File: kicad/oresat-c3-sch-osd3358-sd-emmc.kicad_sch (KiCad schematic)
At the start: 65 parts, among them J4 DM3BT-DSF-PEJS, U1 OSD3358-512M-BSM, U8 TCAN330, U9 EMMC+RESET+5.1-COMPATIBLE-BA

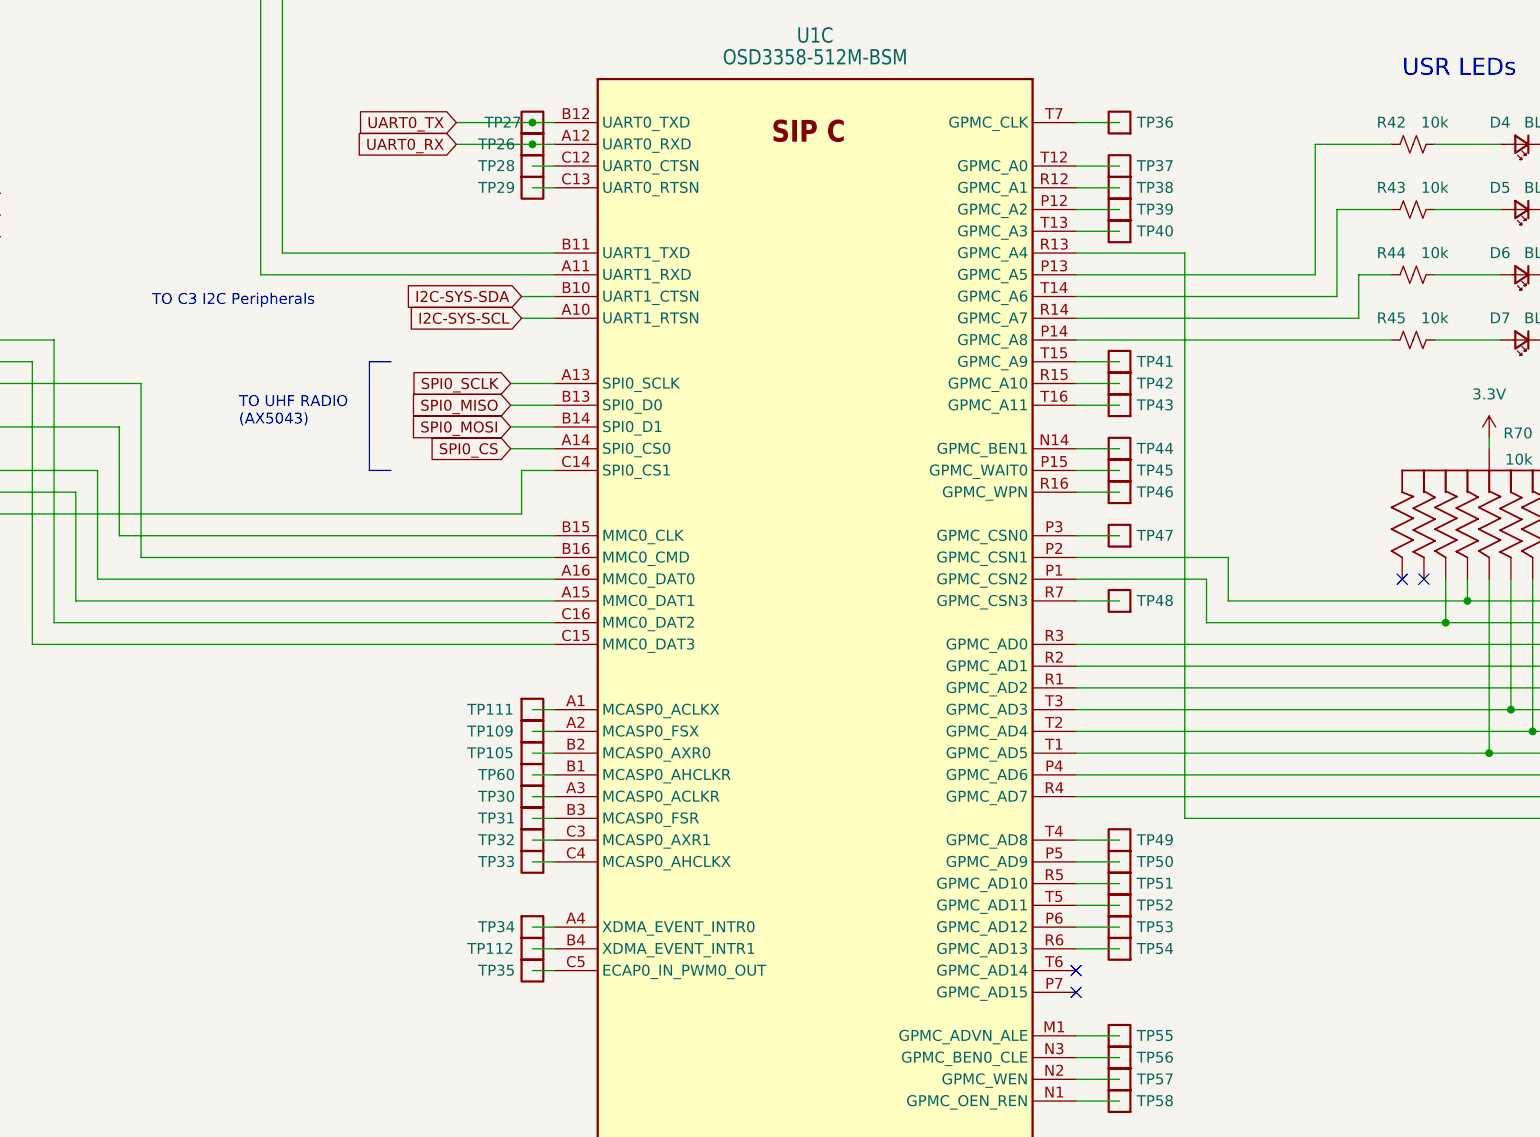
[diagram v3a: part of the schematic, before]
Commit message: Rough draft schematic of C3 v6 done. L band fixed, some GPIO attached, awaiting design review before final attachments.
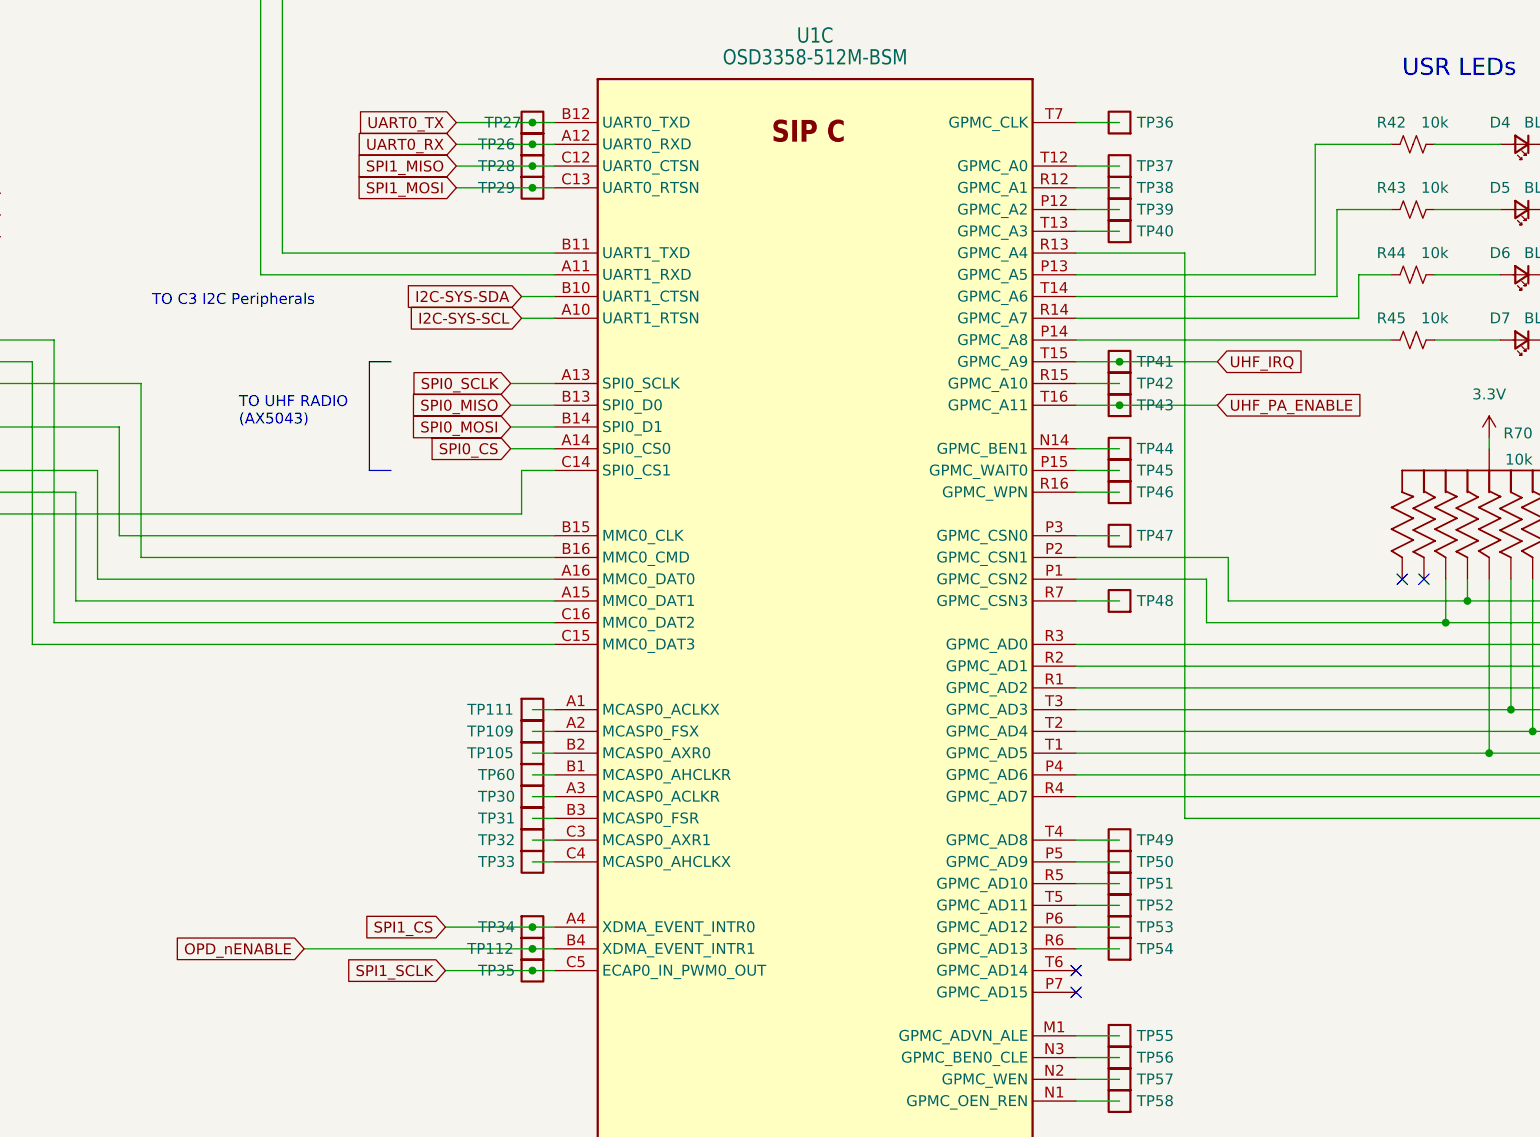
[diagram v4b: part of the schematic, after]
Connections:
- net SPI1_SCLK: now reaches TP35.1, U1.C5 (ECAP0_IN_PWM0_OUT)
- net SPI1_CS: now reaches TP34.1, U1.A4 (XDMA_EVENT_INTR0)
- net OPD_nENABLE: now reaches TP112.1, U1.B4 (XDMA_EVENT_INTR1)
- net SPI1_MISO: now reaches TP28.1, U1.C12 (UART0_CTSN)
- net SPI1_MOSI: now reaches TP29.1, U1.C13 (UART0_RTSN)
- net UHF_IRQ: now reaches TP41.1, U1.T15 (GPMC_A9)
- net UHF_PA_ENABLE: now reaches TP43.1, U1.T16 (GPMC_A11)
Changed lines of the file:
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@@
     (rev "6.0")
   )
+  (junction (at 160.02 106.68) (diameter 0) (color 0 0 0 0)
+  )
   (junction (at 91.44 142.24) (diameter 0) (color 0 0 0 0)
   )
@@
   (junction (at 383.54 167.64) (diameter 0) (color 0 0 0 0)
   )
+  (junction (at 160.02 200.66) (diameter 0) (color 0 0 0 0)
+  )
+  (junction (at 160.02 198.12) (diameter 0) (color 0 0 0 0)
+  )
   (junction (at 284.48 167.64) (diameter 0) (color 0 0 0 0)
   )
@@
   (junction (at 283.21 127) (diameter 0) (color 0 0 0 0)
   )
+  (junction (at 228.6 129.54) (diameter 0) (color 0 0 0 0)
+  )
   (junction (at 93.98 144.78) (diameter 0) (color 0 0 0 0)
   )
@@
   (junction (at 368.3 167.64) (diameter 0) (color 0 0 0 0)
   )
+  (junction (at 160.02 195.58) (diameter 0) (color 0 0 0 0)
+  )
   (junction (at 83.82 129.54) (diameter 0) (color 0 0 0 0)
   )
@@
   (junction (at 81.28 127) (diameter 0) (color 0 0 0 0)
   )
+  (junction (at 160.02 109.22) (diameter 0) (color 0 0 0 0)
+  )
   (junction (at 266.7 160.02) (diameter 0) (color 0 0 0 0)
   )
@@
   )
   (junction (at 283.21 119.38) (diameter 0) (color 0 0 0 0)
+  )
+  (junction (at 228.6 134.62) (diameter 0) (color 0 0 0 0)
   )
   (junction (at 269.24 157.48) (diameter 0) (color 0 0 0 0)
@@
     (stroke (width 0) (type default))
   )
+  (wire (pts (xy 151.13 106.68) (xy 160.02 106.68))
+    (stroke (width 0) (type default))
+  )
   (wire (pts (xy 57.15 106.68) (xy 67.31 106.68))
     (stroke (width 0) (type default))
@@
     (stroke (width 0) (type default))
   )
+  (wire (pts (xy 133.35 198.12) (xy 160.02 198.12))
+    (stroke (width 0) (type default))
+  )
   (wire (pts (xy 265.43 127) (xy 273.05 127))
     (stroke (width 0) (type default))
@@
     (stroke (width 0) (type default))
   )
+  (wire (pts (xy 151.13 109.22) (xy 160.02 109.22))
+    (stroke (width 0) (type default))
+  )
   (wire (pts (xy 157.48 134.62) (xy 162.56 134.62))
     (stroke (width 0) (type default))
@@
     (stroke (width 0) (type default))
   )
+  (wire (pts (xy 228.6 134.62) (xy 240.03 134.62))
+    (stroke (width 0) (type default))
+  )
   (wire (pts (xy 111.76 137.16) (xy 88.9 137.16))
     (stroke (width 0) (type default))
@@
     (stroke (width 0) (type default))
   )
+  (wire (pts (xy 149.86 200.66) (xy 160.02 200.66))
+    (stroke (width 0) (type default))
+  )
   (wire (pts (xy 106.68 144.78) (xy 106.68 157.48))
     (stroke (width 0) (type default))
@@
     (stroke (width 0) (type default))
   )
+  (wire (pts (xy 228.6 129.54) (xy 240.03 129.54))
+    (stroke (width 0) (type default))
+  )
   (wire (pts (xy 55.88 152.4) (xy 55.88 153.67))
     (stroke (width 0) (type default))
@@
   )
   (wire (pts (xy 130.81 64.77) (xy 130.81 116.84))
+    (stroke (width 0) (type default))
+  )
+  (wire (pts (xy 149.86 195.58) (xy 160.02 195.58))
     (stroke (width 0) (type default))
   )
@@
     (effects (font (size 1.27 1.27)) (justify left bottom))
   )
+  (global_label "SPI1_CS" (shape input) (at 149.86 195.58 180) (fields_autoplaced)
+    (effects (font (size 1.27 1.27)) (justify right))
+    (property "Intersheetrefs" "${INTERSHEET_REFS}" (at 139.2133 195.58 0)
+      (effects (font (size 1.27 1.27)) (justify right))
+    )
+  )
   (global_label "SPI0_MOSI" (shape input) (at 157.48 137.16 180) (fields_autoplaced)
     (effects (font (size 1.27 1.27)) (justify right))
@@
     )
   )
+  (global_label "SPI1_MISO" (shape input) (at 151.13 106.68 180) (fields_autoplaced)
+    (effects (font (size 1.27 1.27)) (justify right))
+    (property "Intersheetrefs" "${INTERSHEET_REFS}" (at 138.3666 106.68 0)
+      (effects (font (size 1.27 1.27)) (justify right))
+    )
+  )
+  (global_label "UHF_IRQ" (shape input) (at 240.03 129.54 0) (fields_autoplaced)
+    (effects (font (size 1.27 1.27)) (justify left))
+    (property "Intersheetrefs" "${INTERSHEET_REFS}" (at 250.8583 129.54 0)
+      (effects (font (size 1.27 1.27)) (justify left))
+    )
+  )
   (global_label "SPI0_SCLK" (shape input) (at 157.48 132.08 180) (fields_autoplaced)
     (effects (font (size 1.27 1.27)) (justify right))
@@
     )
   )
+  (global_label "OPD_nENABLE" (shape input) (at 133.35 198.12 180) (fields_autoplaced)
+    (effects (font (size 1.27 1.27)) (justify right))
+    (property "Intersheetrefs" "${INTERSHEET_REFS}" (at 117.4419 198.12 0)
+      (effects (font (size 1.27 1.27)) (justify right))
+    )
+  )
   (global_label "SPI0_MISO" (shape input) (at 157.48 134.62 180) (fields_autoplaced)
     (effects (font (size 1.27 1.27)) (justify right))
@@
     )
   )
+  (global_label "UHF_PA_ENABLE" (shape input) (at 240.03 134.62 0) (fields_autoplaced)
+    (effects (font (size 1.27 1.27)) (justify left))
+    (property "Intersheetrefs" "${INTERSHEET_REFS}" (at 257.9944 134.62 0)
+      (effects (font (size 1.27 1.27)) (justify left))
+    )
+  )
   (global_label "UART0_RX" (shape input) (at 151.13 104.14 180) (fields_autoplaced)
     (effects (font (size 1.27 1.27)) (justify right))
@@
     (effects (font (size 1.27 1.27)) (justify right))
     (property "Intersheetrefs" "${INTERSHEET_REFS}" (at 146.8333 139.7 0)
+      (effects (font (size 1.27 1.27)) (justify right))
+    )
+  )
+  (global_label "SPI1_SCLK" (shape input) (at 149.86 200.66 180) (fields_autoplaced)
+    (effects (font (size 1.27 1.27)) (justify right))
+    (property "Intersheetrefs" "${INTERSHEET_REFS}" (at 136.9152 200.66 0)
       (effects (font (size 1.27 1.27)) (justify right))
     )
@@
     )
   )
+  (global_label "SPI1_MOSI" (shape input) (at 151.13 109.22 180) (fields_autoplaced)
+    (effects (font (size 1.27 1.27)) (justify right))
+    (property "Intersheetrefs" "${INTERSHEET_REFS}" (at 138.3666 109.22 0)
+      (effects (font (size 1.27 1.27)) (justify right))
+    )
+  )

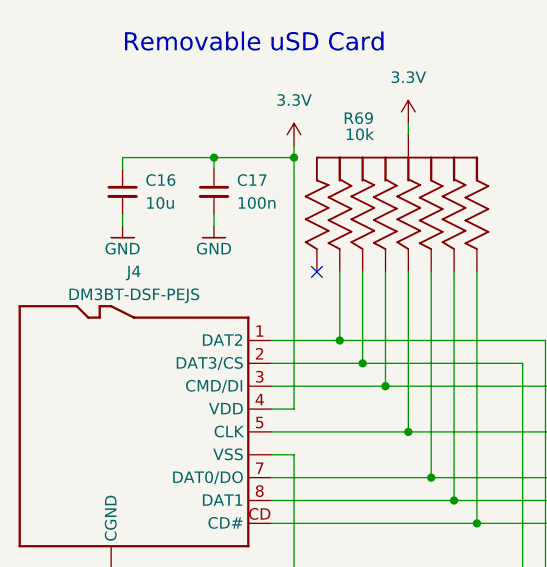
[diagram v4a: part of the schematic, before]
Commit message: First round of ERC fixes.
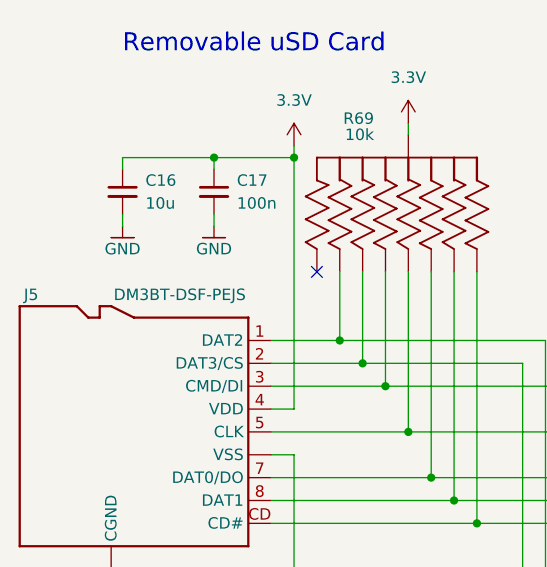
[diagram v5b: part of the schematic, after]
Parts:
- renumbered J4 to J5
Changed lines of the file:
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@@
   )
   (symbol (lib_id "J-Hirose-DM3BT-DSF-PEJS-sd-connector:DM3BT-DSF-PEJS") (at 58.42 137.16 0) (mirror y) (unit 1)
-    (in_bom yes) (on_board yes) (dnp no) (fields_autoplaced)
-    (property "Reference" "J4" (at 58.42 119.38 0)
+    (in_bom yes) (on_board yes) (dnp no)
+    (property "Reference" "J5" (at 46.99 121.92 0)
       (effects (font (size 1.27 1.27)))
     )
-    (property "Value" "DM3BT-DSF-PEJS" (at 58.42 121.92 0)
+    (property "Value" "DM3BT-DSF-PEJS" (at 63.5 121.92 0)
       (effects (font (size 1.27 1.27)))
     )
@@
       (project "oresat-c3"
         (path "/65d12cdd-c326-4033-9053-c59fa4e0b25e/f3d147ad-4cea-4d77-ae60-95882b03454e"
-          (reference "J4") (unit 1)
+          (reference "J5") (unit 1)
         )
       )

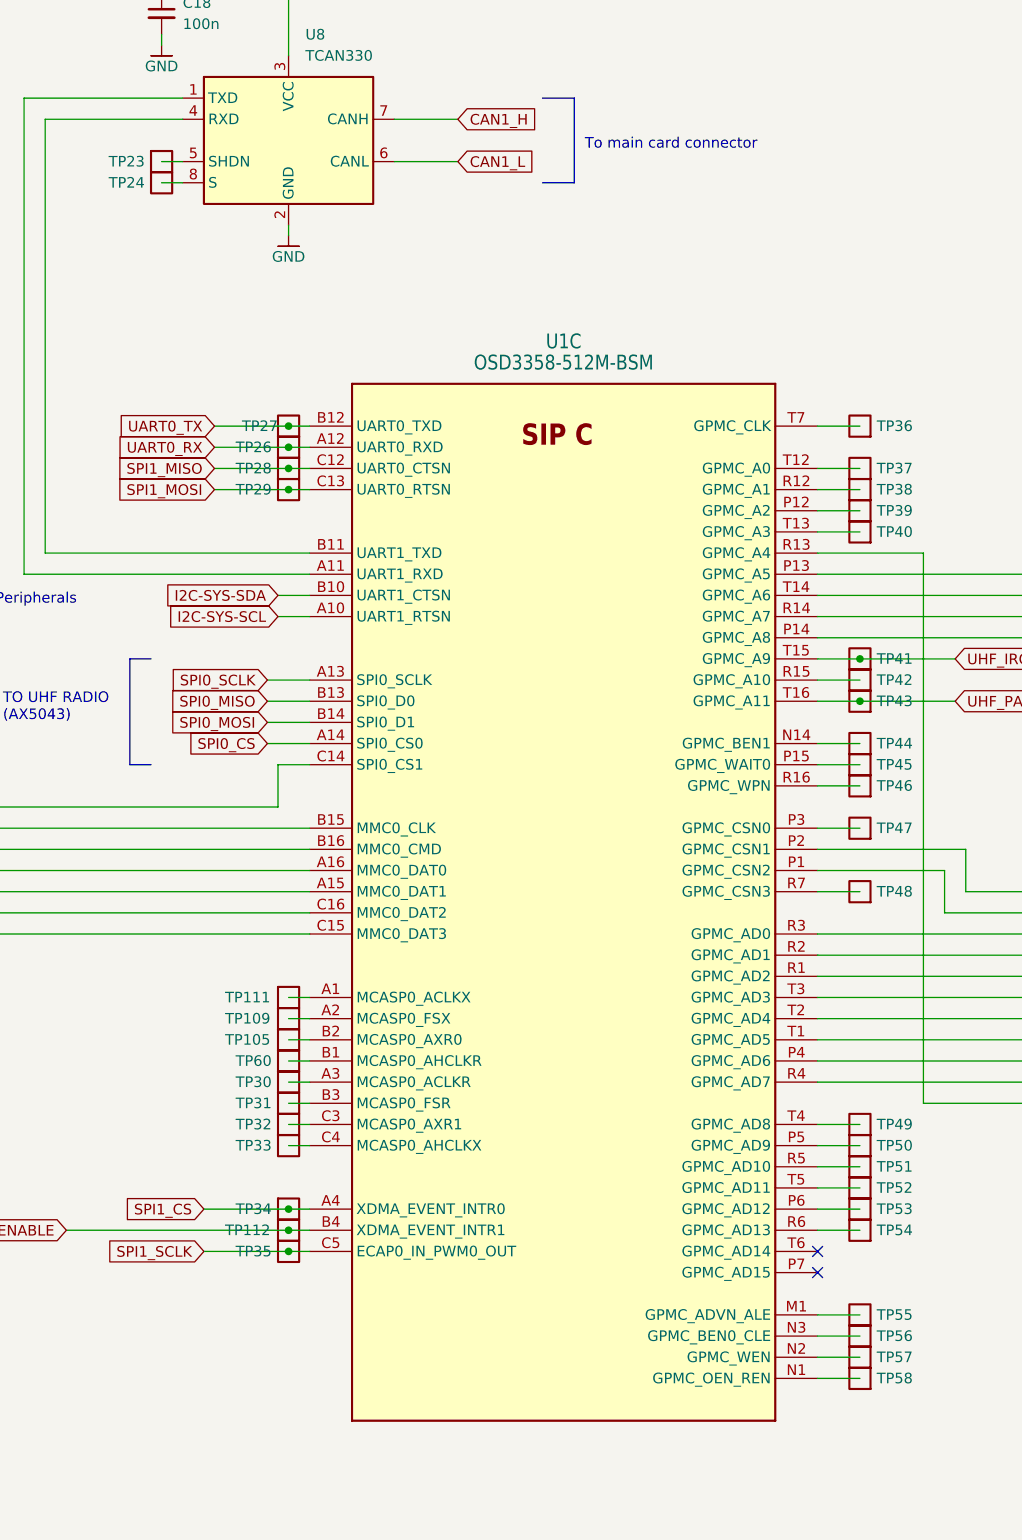
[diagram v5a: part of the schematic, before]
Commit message: Sane amount of ERC errors now; mostly library cleanups.
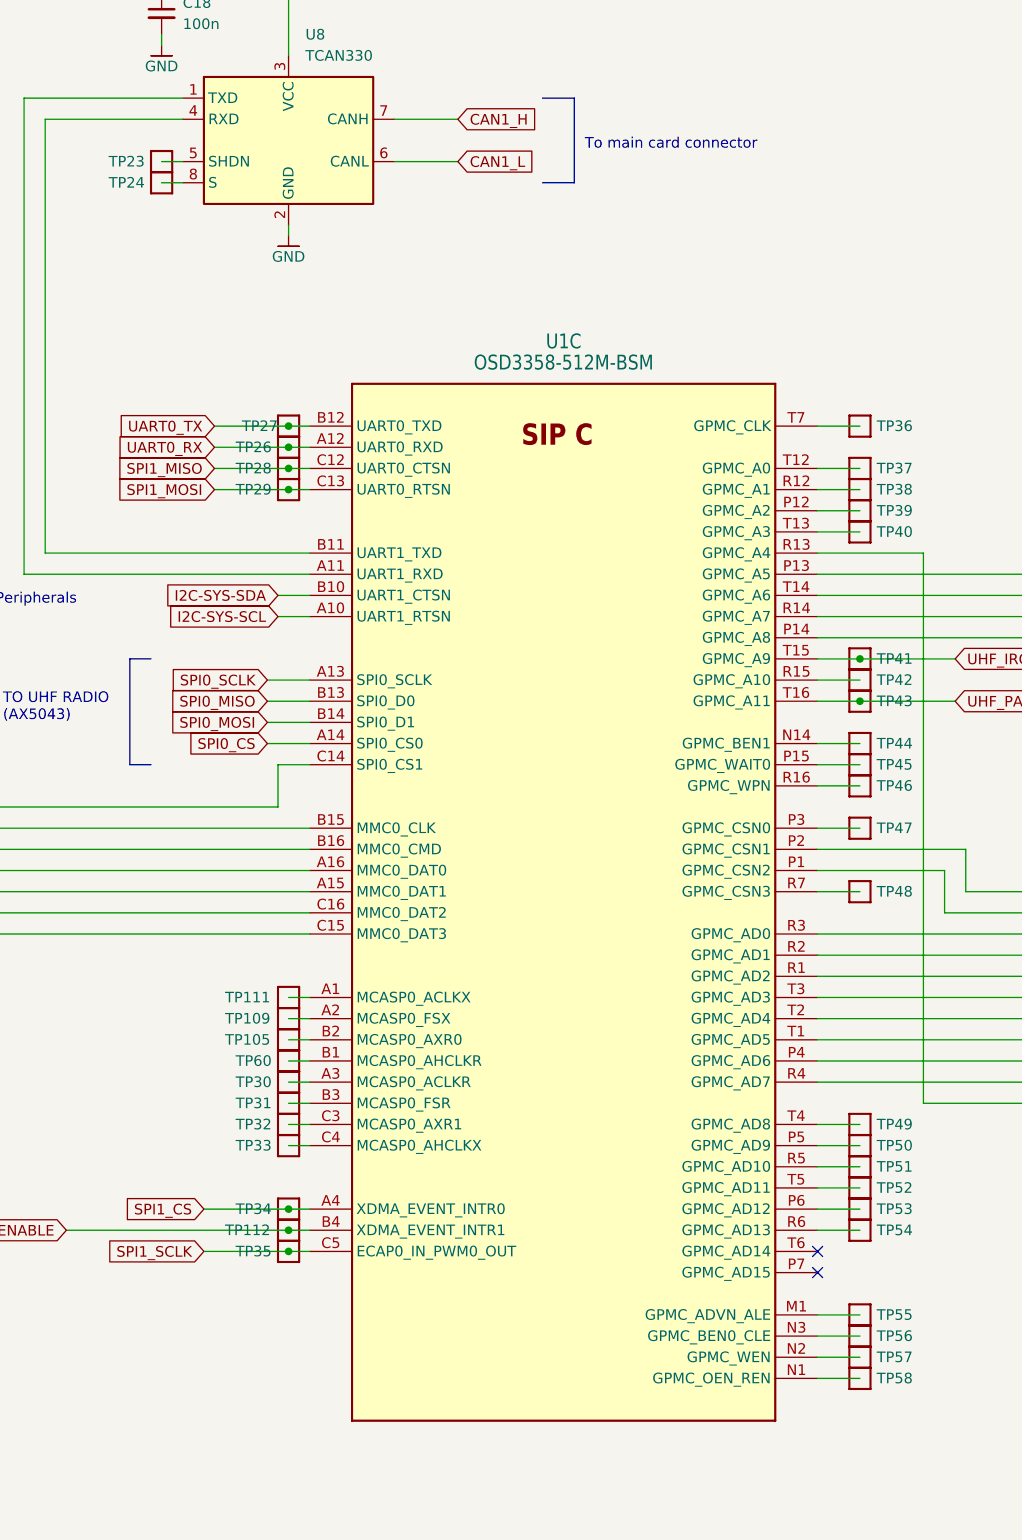
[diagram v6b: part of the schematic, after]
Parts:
- J5: symbol J-Hirose-DM3BT-DSF-PEJS-sd-connector:DM3BT-DSF-PEJS -> oresat-connectors:DM3BT-DSF-PEJS
- R69, R70, R71: symbol R-EXB-A10P391j:EXB-A10P391J -> oresat-passives:EXB-A10P391J
- TP105, TP109, TP111, TP112, TP23, TP24, TP26, TP27, TP28, TP29, TP30, TP31, TP32, TP33, TP34, TP35, TP36, TP37, TP38, TP39, TP40, TP41, TP42, TP43, TP44, TP45, TP46, TP47, TP48, TP49, TP50, TP51, TP52, TP53, TP54, TP55, TP56, TP57, TP58, TP60: footprint OreSat-TestPoint:PAD.03X.04 -> oresat-misc:PAD.03X.04; symbol OreSat-TestPoint:Test-Point -> oresat-misc:Test-Point
